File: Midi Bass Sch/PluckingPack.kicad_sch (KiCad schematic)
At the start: 42 parts, among them Q1 BDW93C, Q2 BDW93C, Q3 BDW93C, Q4 BDW93C, Q5 BDW93C, Q6 BDW93C, Q7 BDW93C, Q8 BDW93C, U12 LTV-247, U13 LTV-247

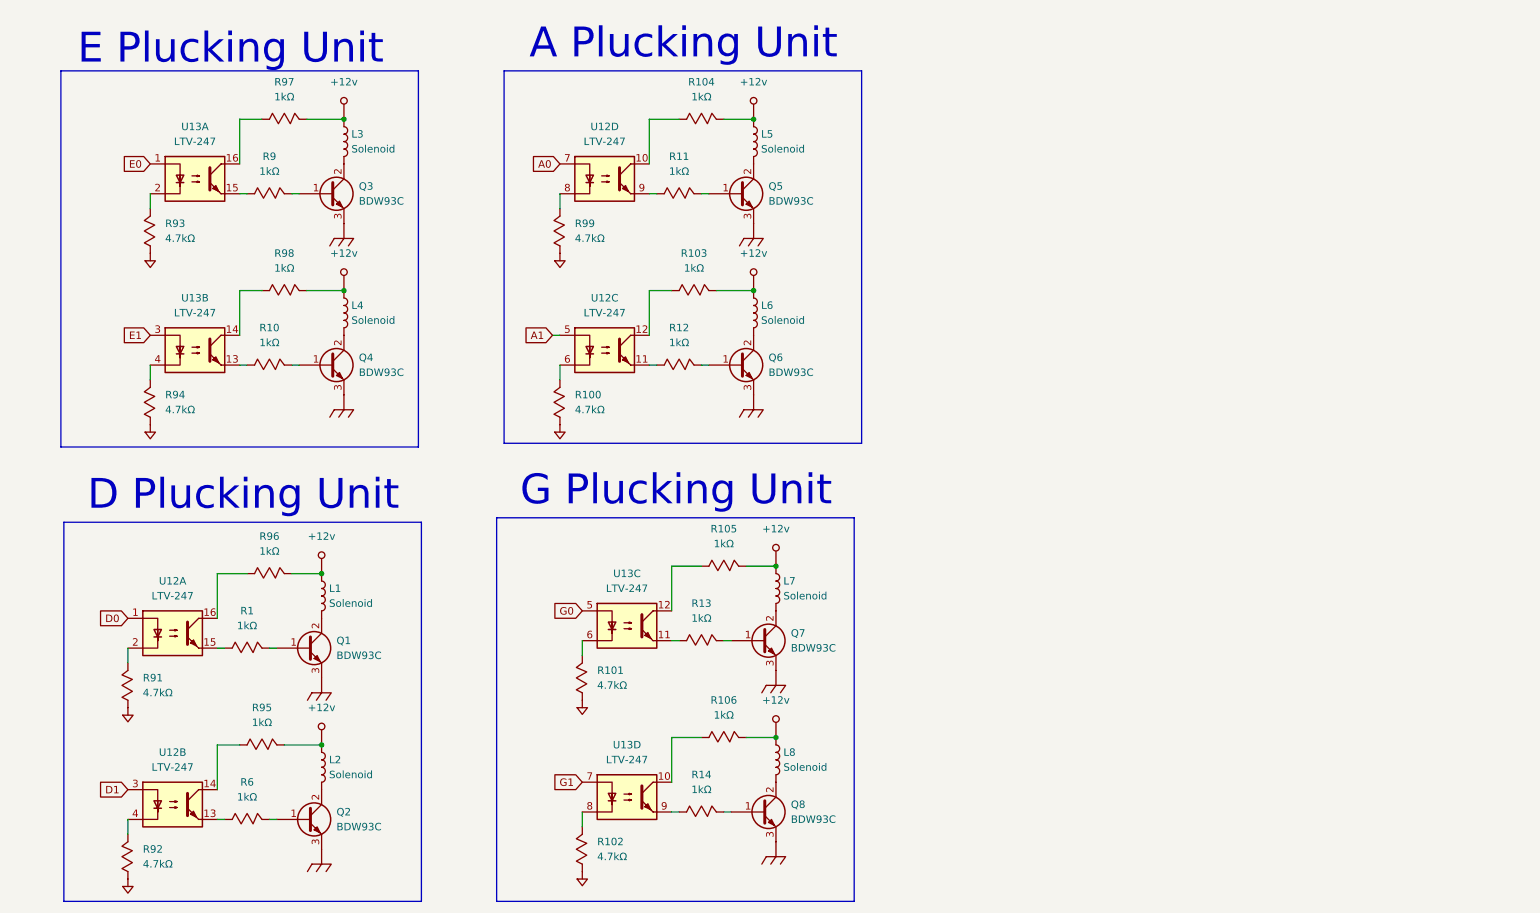
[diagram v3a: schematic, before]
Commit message: added solenoid array for the A slave
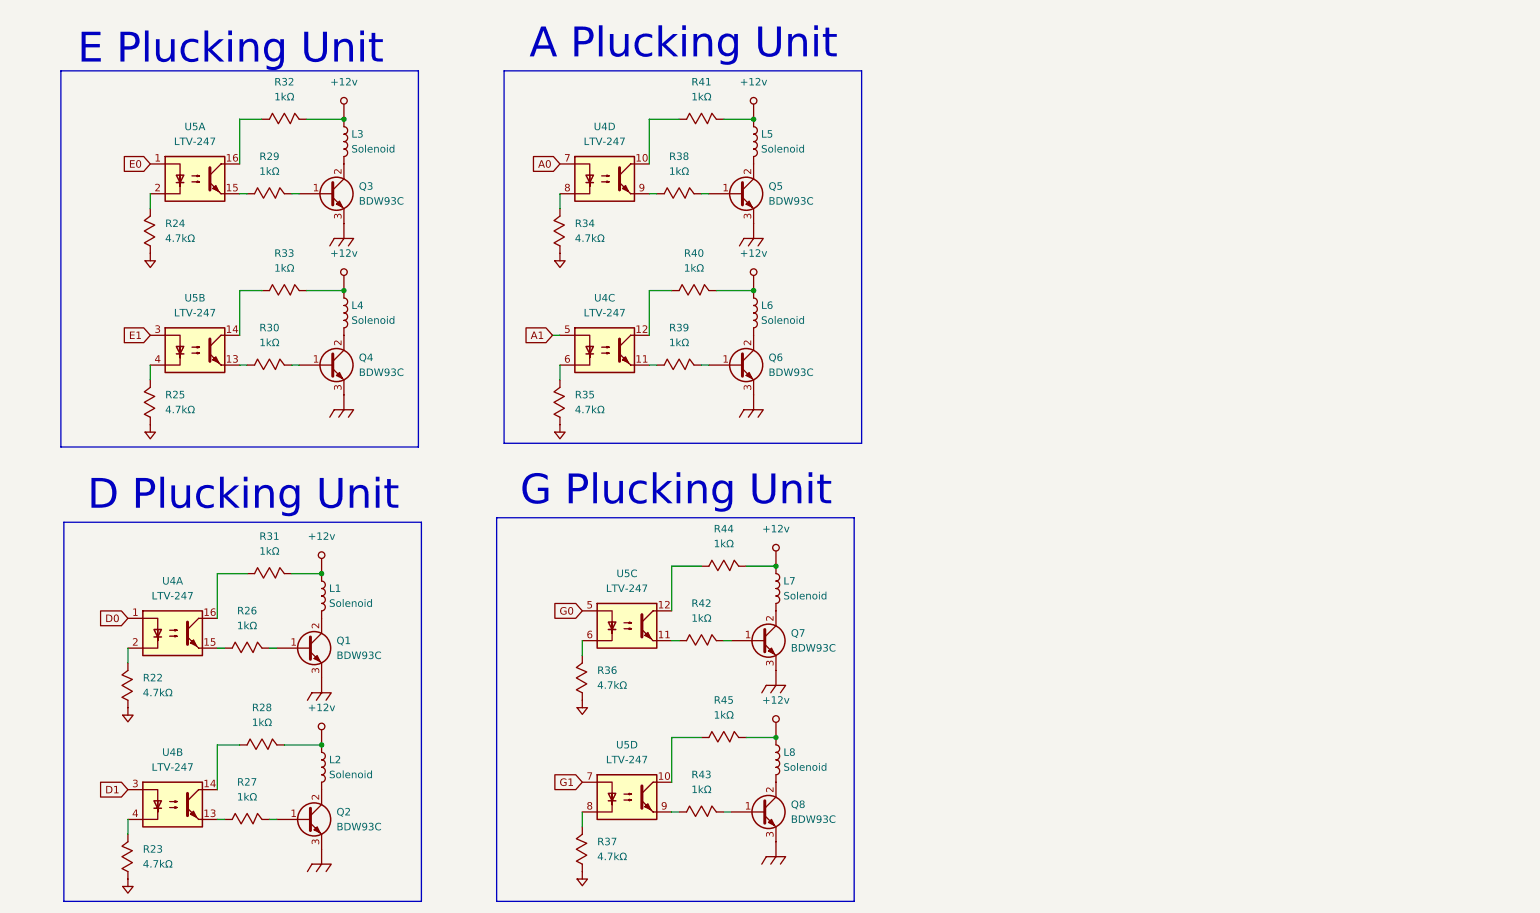
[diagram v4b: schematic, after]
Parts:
- renumbered R91 to R22, R92 to R23, R93 to R24, R94 to R25, R1 to R26, R6 to R27, R95 to R28, R9 to R29, R10 to R30, R96 to R31, R97 to R32, R98 to R33, R99 to R34, R100 to R35, R101 to R36, R102 to R37, R11 to R38, R12 to R39, R103 to R40, R104 to R41, R13 to R42, R14 to R43, R105 to R44, R106 to R45, U12 to U4, U13 to U5

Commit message: added footprints to kicad schematic still need footprint for din connector
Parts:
- Q1, Q2, Q3, Q4, Q5, Q6, Q7, Q8: footprint (none) -> Package_TO_SOT_THT:TO-220-3_Vertical
- R22, R23, R24, R25, R26, R27, R28, R29, R30, R31, R32, R33, R34, R35, R36, R37, R38, R39, R40, R41, R42, R43, R44, R45: footprint (none) -> Resistor_SMD:R_0805_2012Metric_Pad1.20x1.40mm_HandSolder
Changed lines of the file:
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@@
 			)
 		)
-		(property "Footprint" ""
+		(property "Footprint" "Resistor_SMD:R_0805_2012Metric_Pad1.20x1.40mm_HandSolder"
 			(at 132.08 59.69 0)
 			(effects
@@
 			)
 		)
-		(property "Footprint" ""
+		(property "Footprint" "Resistor_SMD:R_0805_2012Metric_Pad1.20x1.40mm_HandSolder"
 			(at 55.88 120.65 0)
 			(effects
@@
 			)
 		)
-		(property "Footprint" ""
+		(property "Footprint" "Resistor_SMD:R_0805_2012Metric_Pad1.20x1.40mm_HandSolder"
 			(at 111.76 129.54 0)
 			(effects
@@
 			)
 		)
-		(property "Footprint" ""
+		(property "Footprint" "Resistor_SMD:R_0805_2012Metric_Pad1.20x1.40mm_HandSolder"
 			(at 129.54 72.39 0)
 			(effects
@@
 			)
 		)
-		(property "Footprint" ""
+		(property "Footprint" "Resistor_SMD:R_0805_2012Metric_Pad1.20x1.40mm_HandSolder"
 			(at 133.35 30.48 0)
 			(effects
@@
 			)
 		)
-		(property "Footprint" ""
+		(property "Footprint" "Package_TO_SOT_THT:TO-220-3_Vertical"
 			(at 146.05 72.39 0)
 			(effects
@@
 			)
 		)
-		(property "Footprint" ""
+		(property "Footprint" "Package_TO_SOT_THT:TO-220-3_Vertical"
 			(at 72.39 120.65 0)
 			(effects
@@
 			)
 		)
-		(property "Footprint" ""
+		(property "Footprint" "Resistor_SMD:R_0805_2012Metric_Pad1.20x1.40mm_HandSolder"
 			(at 107.95 53.34 0)
 			(effects
@@
 			)
 		)
-		(property "Footprint" ""
+		(property "Footprint" "Resistor_SMD:R_0805_2012Metric_Pad1.20x1.40mm_HandSolder"
 			(at 111.76 158.75 0)
 			(effects
@@
 			)
 		)
-		(property "Footprint" ""
+		(property "Footprint" "Resistor_SMD:R_0805_2012Metric_Pad1.20x1.40mm_HandSolder"
 			(at 34.29 130.81 0)
 			(effects
@@
 			)
 		)
-		(property "Footprint" ""
+		(property "Footprint" "Resistor_SMD:R_0805_2012Metric_Pad1.20x1.40mm_HandSolder"
 			(at 59.69 43.18 0)
 			(effects
@@
 			)
 		)
-		(property "Footprint" ""
+		(property "Footprint" "Resistor_SMD:R_0805_2012Metric_Pad1.20x1.40mm_HandSolder"
 			(at 137.16 135.89 0)
 			(effects
@@
 			)
 		)
-		(property "Footprint" ""
+		(property "Footprint" "Package_TO_SOT_THT:TO-220-3_Vertical"
 			(at 149.86 148.59 0)
 			(effects
@@
 			)
 		)
-		(property "Footprint" ""
+		(property "Footprint" "Resistor_SMD:R_0805_2012Metric_Pad1.20x1.40mm_HandSolder"
 			(at 59.69 72.39 0)
 			(effects
@@
 			)
 		)
-		(property "Footprint" ""
+		(property "Footprint" "Package_TO_SOT_THT:TO-220-3_Vertical"
 			(at 76.2 72.39 0)
 			(effects
@@
 			)
 		)
-		(property "Footprint" ""
+		(property "Footprint" "Resistor_SMD:R_0805_2012Metric_Pad1.20x1.40mm_HandSolder"
 			(at 137.16 106.68 0)
 			(effects
@@
 			)
 		)
-		(property "Footprint" ""
+		(property "Footprint" "Resistor_SMD:R_0805_2012Metric_Pad1.20x1.40mm_HandSolder"
 			(at 133.35 148.59 0)
 			(effects
@@
 			)
 		)
-		(property "Footprint" ""
+		(property "Footprint" "Resistor_SMD:R_0805_2012Metric_Pad1.20x1.40mm_HandSolder"
 			(at 59.69 107.95 0)
 			(effects
@@
 			)
 		)
-		(property "Footprint" ""
+		(property "Footprint" "Resistor_SMD:R_0805_2012Metric_Pad1.20x1.40mm_HandSolder"
 			(at 58.42 137.16 0)
 			(effects
@@
 			)
 		)
-		(property "Footprint" ""
+		(property "Footprint" "Resistor_SMD:R_0805_2012Metric_Pad1.20x1.40mm_HandSolder"
 			(at 129.54 43.18 0)
 			(effects
@@
 			)
 		)
-		(property "Footprint" ""
+		(property "Footprint" "Resistor_SMD:R_0805_2012Metric_Pad1.20x1.40mm_HandSolder"
 			(at 133.35 119.38 0)
 			(effects
@@
 			)
 		)
-		(property "Footprint" ""
+		(property "Footprint" "Resistor_SMD:R_0805_2012Metric_Pad1.20x1.40mm_HandSolder"
 			(at 62.23 59.69 0)
 			(effects
@@
 			)
 		)
-		(property "Footprint" ""
+		(property "Footprint" "Package_TO_SOT_THT:TO-220-3_Vertical"
 			(at 72.39 149.86 0)
 			(effects
@@
 			)
 		)
-		(property "Footprint" ""
+		(property "Footprint" "Package_TO_SOT_THT:TO-220-3_Vertical"
 			(at 76.2 43.18 0)
 			(effects
@@
 			)
 		)
-		(property "Footprint" ""
+		(property "Footprint" "Resistor_SMD:R_0805_2012Metric_Pad1.20x1.40mm_HandSolder"
 			(at 38.1 53.34 0)
 			(effects
@@
 			)
 		)
-		(property "Footprint" ""
+		(property "Footprint" "Resistor_SMD:R_0805_2012Metric_Pad1.20x1.40mm_HandSolder"
 			(at 38.1 82.55 0)
 			(effects
@@
 			)
 		)
-		(property "Footprint" ""
+		(property "Footprint" "Resistor_SMD:R_0805_2012Metric_Pad1.20x1.40mm_HandSolder"
 			(at 62.23 30.48 0)
 			(effects
@@
 			)
 		)
-		(property "Footprint" ""
+		(property "Footprint" "Resistor_SMD:R_0805_2012Metric_Pad1.20x1.40mm_HandSolder"
 			(at 55.88 149.86 0)
 			(effects
@@
 			)
 		)
-		(property "Footprint" ""
+		(property "Footprint" "Resistor_SMD:R_0805_2012Metric_Pad1.20x1.40mm_HandSolder"
 			(at 34.29 160.02 0)
 			(effects
@@
 			)
 		)
-		(property "Footprint" ""
+		(property "Footprint" "Resistor_SMD:R_0805_2012Metric_Pad1.20x1.40mm_HandSolder"
 			(at 107.95 82.55 0)
 			(effects
@@
 			)
 		)
-		(property "Footprint" ""
+		(property "Footprint" "Package_TO_SOT_THT:TO-220-3_Vertical"
 			(at 146.05 43.18 0)
 			(effects
@@
 			)
 		)
-		(property "Footprint" ""
+		(property "Footprint" "Package_TO_SOT_THT:TO-220-3_Vertical"
 			(at 149.86 119.38 0)
 			(effects

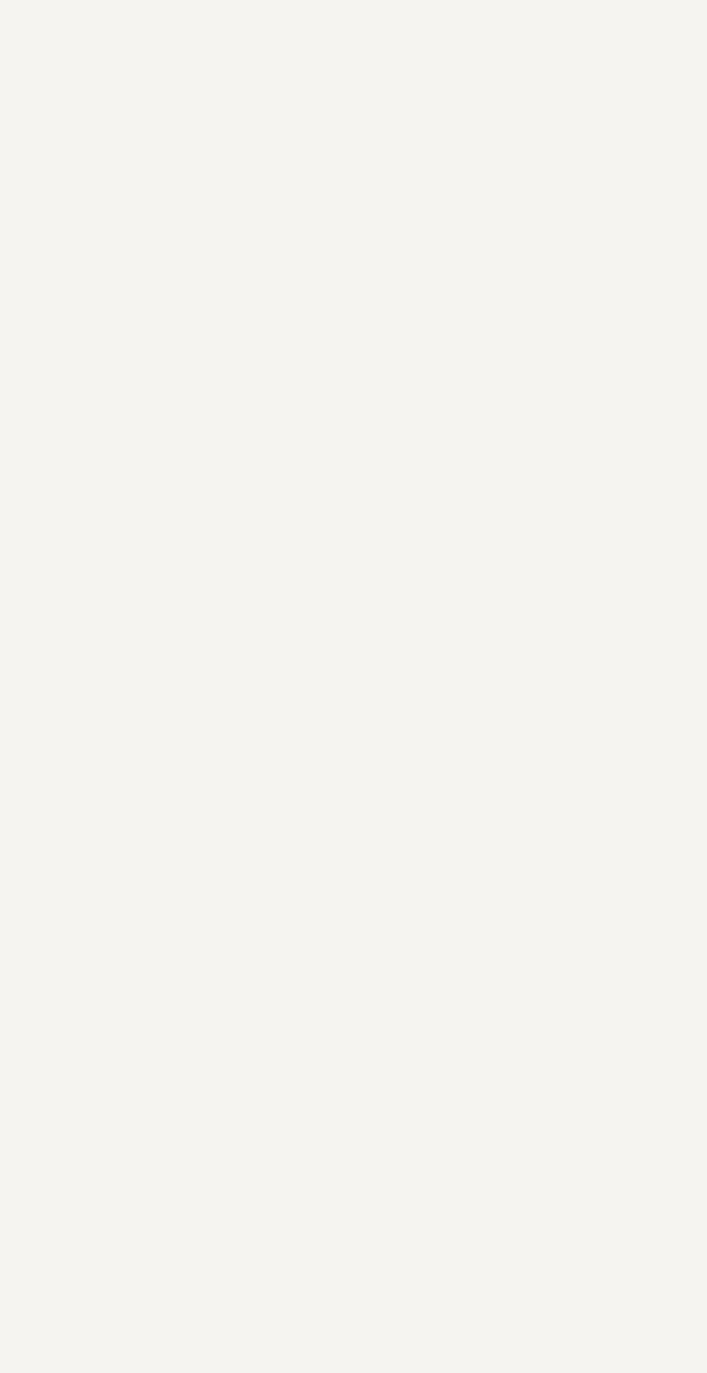
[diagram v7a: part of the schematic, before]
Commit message: began adding mute application to plucking unit
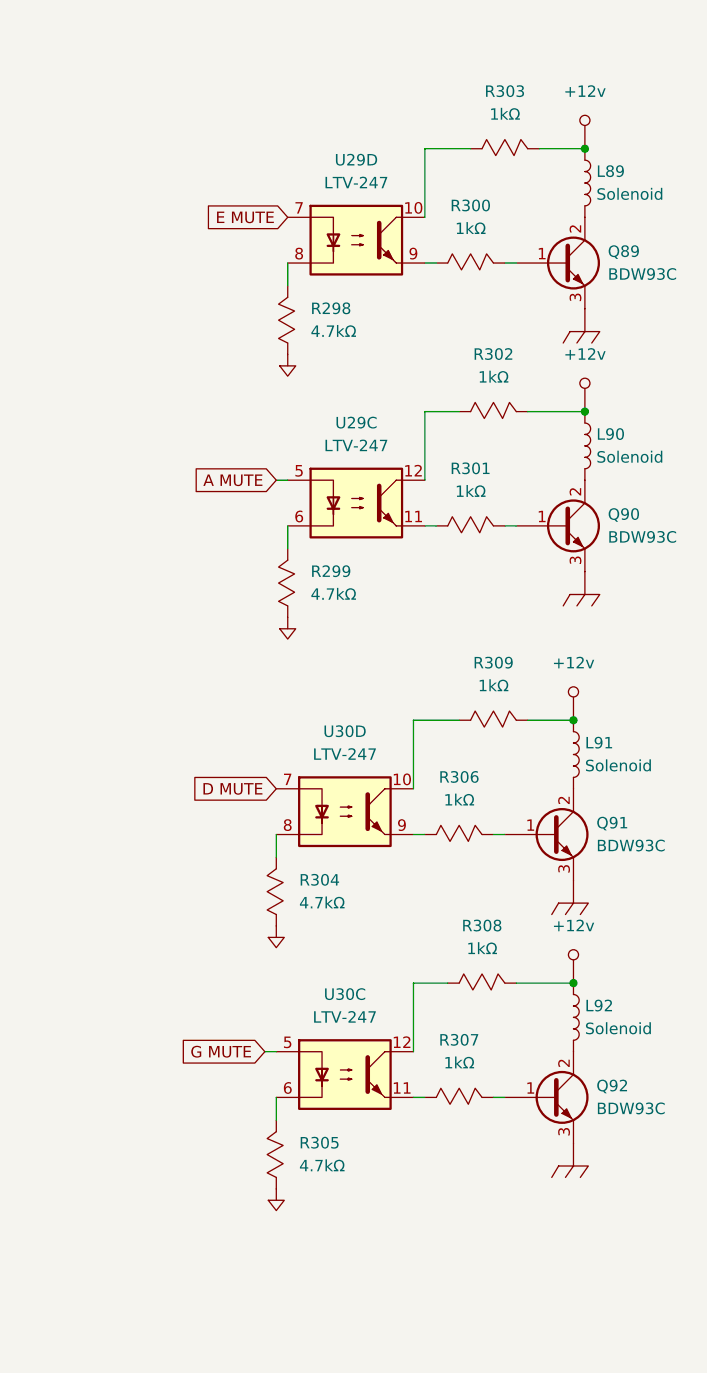
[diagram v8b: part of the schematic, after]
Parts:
- added L89, L90, L91, L92: Solenoid, symbol Device:L
- added Q89, Q90, Q91, Q92: BDW93C, Package_TO_SOT_THT:TO-220-3_Vertical, symbol Device:Q_NPN_BCE
- added R298, R299, R304, R305: 4.7kΩ, Resistor_SMD:R_0805_2012Metric_Pad1.20x1.40mm_HandSolder, symbol Custom Symbols:Resistor_Mod
- added R300, R301, R302, R303, R306, R307, R308, R309: 1kΩ, Resistor_SMD:R_0805_2012Metric_Pad1.20x1.40mm_HandSolder, symbol Custom Symbols:Resistor_Mod
- added U29, U30: LTV-247, Package_SO:SOP-16_4.4x10.4mm_P1.27mm, symbol Isolator:LTV-247
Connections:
- net +12v: now also L89.1, L90.1, L91.1, L92.1, R302.2, R303.2, R308.2, R309.2
- net Chassis_GND: now also Q89.3 (E), Q90.3 (E), Q91.3 (E), Q92.3 (E)
- net GND: now also R298.1, R299.1, R304.1, R305.1
- new net: R301.1, U29.11
- new net: Q90.1 (B), R301.2
- new net: R302.1, U29.12
- new net: R309.1, U30.10
- new net: L92.2, Q92.2 (C)
- new net: Q91.1 (B), R306.2
- new net: L91.2, Q91.2 (C)
- new net: L89.2, Q89.2 (C)
- new net: R305.2, U30.6
- new net: R299.2, U29.6
- new net: Q89.1 (B), R300.2
- new net: R303.1, U29.10
- new net: R298.2, U29.8
- new net: R300.1, U29.9
- new net: R308.1, U30.12
- new net: R304.2, U30.8
- new net: R306.1, U30.9
- new net: Q92.1 (B), R307.2
- new net: R307.1, U30.11
- new net: L90.2, Q90.2 (C)
- new net A MUTE: U29.5
- new net D MUTE: U30.7
- new net E MUTE: U29.7
- new net G MUTE: U30.5
